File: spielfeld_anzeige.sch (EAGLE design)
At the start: 32 parts, among them IC1 UDN2981A, IC2 UDN2981A, IC3 74HC595N, IC4 74HC595N, IC5 74HC595N

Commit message: Layout fertig
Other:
- note removed: "colon data better here?!"
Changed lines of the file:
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@@
 <grid distance="0.1" unitdist="inch" unit="inch" style="lines" multiple="1" display="no" altdistance="0.01" altunitdist="inch" altunit="inch"/>
 <layers>
-<layer number="1" name="Top" color="4" fill="1" visible="yes" active="no"/>
-<layer number="16" name="Bottom" color="1" fill="1" visible="yes" active="no"/>
-<layer number="17" name="Pads" color="2" fill="1" visible="yes" active="no"/>
-<layer number="18" name="Vias" color="2" fill="1" visible="yes" active="no"/>
-<layer number="19" name="Unrouted" color="6" fill="1" visible="yes" active="no"/>
-<layer number="20" name="Dimension" color="15" fill="1" visible="yes" active="no"/>
-<layer number="21" name="tPlace" color="7" fill="1" visible="yes" active="no"/>
-<layer number="22" name="bPlace" color="7" fill="1" visible="yes" active="no"/>
-<layer number="23" name="tOrigins" color="15" fill="1" visible="yes" active="no"/>
-<layer number="24" name="bOrigins" color="15" fill="1" visible="yes" active="no"/>
-<layer number="25" name="tNames" color="7" fill="1" visible="yes" active="no"/>
-<layer number="26" name="bNames" color="7" fill="1" visible="yes" active="no"/>
-<layer number="27" name="tValues" color="7" fill="1" visible="yes" active="no"/>
-<layer number="28" name="bValues" color="7" fill="1" visible="yes" active="no"/>
+<layer number="1" name="Top" color="4" fill="1" visible="no" active="no"/>
+<layer number="16" name="Bottom" color="1" fill="1" visible="no" active="no"/>
+<layer number="17" name="Pads" color="2" fill="1" visible="no" active="no"/>
+<layer number="18" name="Vias" color="2" fill="1" visible="no" active="no"/>
+<layer number="19" name="Unrouted" color="6" fill="1" visible="no" active="no"/>
+<layer number="20" name="Dimension" color="15" fill="1" visible="no" active="no"/>
+<layer number="21" name="tPlace" color="7" fill="1" visible="no" active="no"/>
+<layer number="22" name="bPlace" color="7" fill="1" visible="no" active="no"/>
+<layer number="23" name="tOrigins" color="15" fill="1" visible="no" active="no"/>
+<layer number="24" name="bOrigins" color="15" fill="1" visible="no" active="no"/>
+<layer number="25" name="tNames" color="7" fill="1" visible="no" active="no"/>
+<layer number="26" name="bNames" color="7" fill="1" visible="no" active="no"/>
+<layer number="27" name="tValues" color="7" fill="1" visible="no" active="no"/>
+<layer number="28" name="bValues" color="7" fill="1" visible="no" active="no"/>
 <layer number="29" name="tStop" color="7" fill="3" visible="no" active="no"/>
 <layer number="30" name="bStop" color="7" fill="6" visible="no" active="no"/>
@@
 <layer number="35" name="tGlue" color="7" fill="4" visible="no" active="no"/>
 <layer number="36" name="bGlue" color="7" fill="5" visible="no" active="no"/>
-<layer number="37" name="tTest" color="7" fill="1" visible="yes" active="no"/>
-<layer number="38" name="bTest" color="7" fill="1" visible="yes" active="no"/>
+<layer number="37" name="tTest" color="7" fill="1" visible="no" active="no"/>
+<layer number="38" name="bTest" color="7" fill="1" visible="no" active="no"/>
 <layer number="39" name="tKeepout" color="4" fill="11" visible="no" active="no"/>
 <layer number="40" name="bKeepout" color="1" fill="11" visible="no" active="no"/>
@@
 <layer number="44" name="Drills" color="7" fill="1" visible="no" active="no"/>
 <layer number="45" name="Holes" color="7" fill="1" visible="no" active="no"/>
-<layer number="46" name="Milling" color="3" fill="1" visible="yes" active="no"/>
-<layer number="47" name="Measures" color="7" fill="1" visible="yes" active="no"/>
-<layer number="48" name="Document" color="7" fill="1" visible="yes" active="no"/>
-<layer number="49" name="Reference" color="7" fill="1" visible="yes" active="no"/>
-<layer number="50" name="dxf" color="7" fill="1" visible="yes" active="no"/>
-<layer number="51" name="tDocu" color="7" fill="1" visible="yes" active="no"/>
-<layer number="52" name="bDocu" color="7" fill="1" visible="yes" active="no"/>
-<layer number="53" name="tPadExt" color="7" fill="1" visible="yes" active="no"/>
-<layer number="54" name="bPadExt" color="1" fill="1" visible="yes" active="no"/>
-<layer number="56" name="wert" color="7" fill="1" visible="yes" active="no"/>
+<layer number="46" name="Milling" color="3" fill="1" visible="no" active="no"/>
+<layer number="47" name="Measures" color="7" fill="1" visible="no" active="no"/>
+<layer number="48" name="Document" color="7" fill="1" visible="no" active="no"/>
+<layer number="49" name="Reference" color="7" fill="1" visible="no" active="no"/>
+<layer number="50" name="dxf" color="7" fill="1" visible="no" active="no"/>
+<layer number="51" name="tDocu" color="7" fill="1" visible="no" active="no"/>
+<layer number="52" name="bDocu" color="7" fill="1" visible="no" active="no"/>
+<layer number="53" name="tPadExt" color="7" fill="1" visible="no" active="no"/>
+<layer number="54" name="bPadExt" color="1" fill="1" visible="no" active="no"/>
+<layer number="56" name="wert" color="7" fill="1" visible="no" active="no"/>
 <layer number="91" name="Nets" color="2" fill="1" visible="yes" active="yes"/>
 <layer number="92" name="Busses" color="1" fill="1" visible="yes" active="yes"/>
@@
 <text x="13.97" y="40.64" size="2.54" layer="97">! Dot Led orientation in schematic symbol is inverse !</text>
 <text x="-128.27" y="-44.45" size="2.54" layer="97">pnp to +5V; column driver</text>
-<text x="-157.48" y="-10.16" size="1.778" layer="97">colon data better here?!</text>
 <wire x1="-203.2" y1="-22.86" x2="-45.72" y2="-22.86" width="0.3048" layer="94"/>
 <wire x1="-45.72" y1="-22.86" x2="-45.72" y2="-43.18" width="0.3048" layer="94"/>
@@
 </sheet>
 </sheets>
+<errors>
+</errors>
 </schematic>
 </drawing>

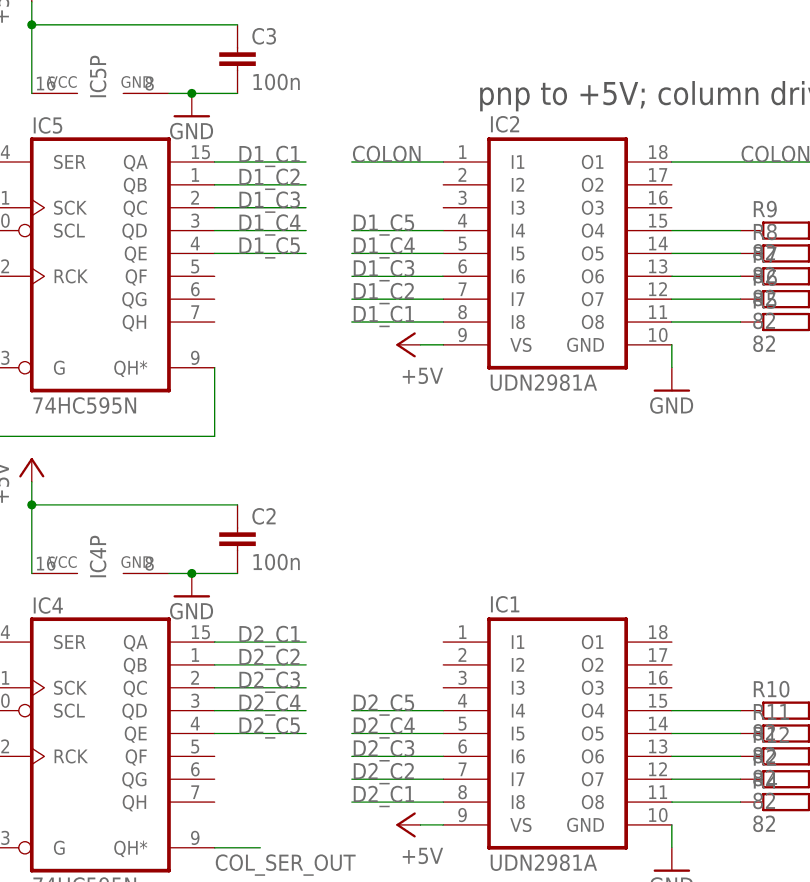
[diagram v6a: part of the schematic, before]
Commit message: Korrekturen Layout
LEDs ins mm-Raster zurückgesetzt.
Maßangaben korrigiert.
Die freien Eingänge der Treiber-ICs mit GND verbunden.
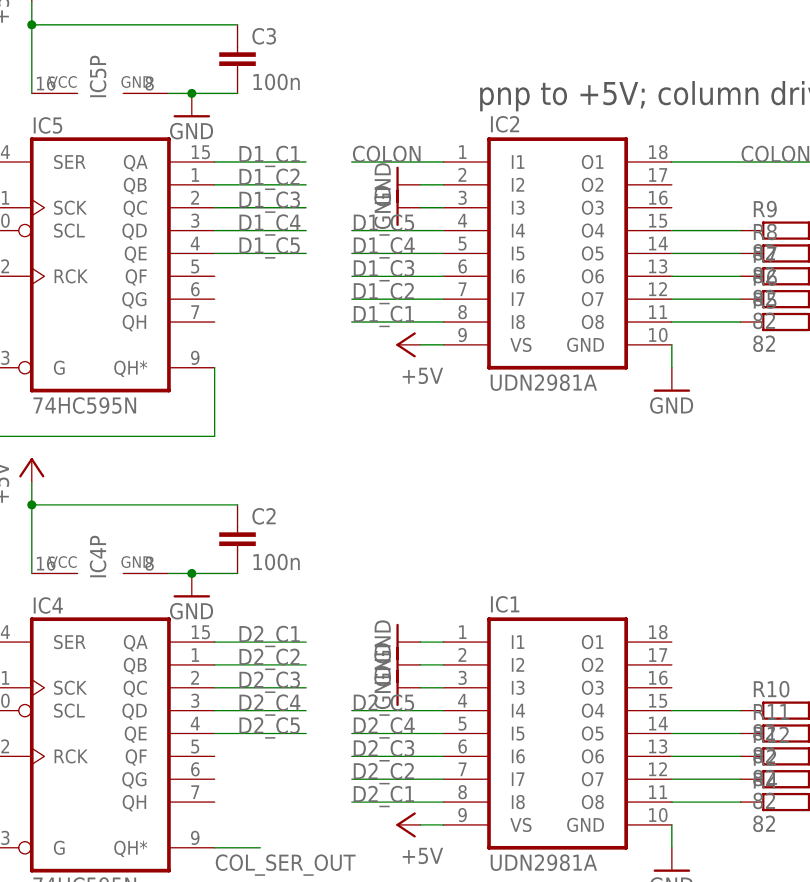
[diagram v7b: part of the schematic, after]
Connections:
- net GND: now also IC1.I1, IC1.I2, IC1.I3, IC2.I2, IC2.I3
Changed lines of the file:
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@@
 <part name="R11" library="rcl" deviceset="R-EU_" device="R0805" value="82"/>
 <part name="R12" library="rcl" deviceset="R-EU_" device="R0805" value="82"/>
+<part name="GND9" library="supply1" deviceset="GND" device=""/>
+<part name="GND10" library="supply1" deviceset="GND" device=""/>
+<part name="GND11" library="supply1" deviceset="GND" device=""/>
+<part name="GND12" library="supply1" deviceset="GND" device=""/>
+<part name="GND14" library="supply1" deviceset="GND" device=""/>
 </parts>
 <sheets>
@@
 <instance part="R11" gate="G$1" x="-93.98" y="-114.3"/>
 <instance part="R12" gate="G$1" x="-93.98" y="-116.84"/>
+<instance part="GND9" gate="1" x="-137.16" y="-53.34" rot="R270"/>
+<instance part="GND10" gate="1" x="-137.16" y="-55.88" rot="R270"/>
+<instance part="GND11" gate="1" x="-137.16" y="-104.14" rot="R270"/>
+<instance part="GND12" gate="1" x="-137.16" y="-106.68" rot="R270"/>
+<instance part="GND14" gate="1" x="-137.16" y="-109.22" rot="R270"/>
 </instances>
 <busses>
@@
 <pinref part="X1" gate="-1" pin="KL"/>
 </segment>
+<segment>
+<pinref part="IC2" gate="1" pin="I2"/>
+<pinref part="GND9" gate="1" pin="GND"/>
+<wire x1="-134.62" y1="-53.34" x2="-132.08" y2="-53.34" width="0.1524" layer="91"/>
+</segment>
+<segment>
+<pinref part="IC2" gate="1" pin="I3"/>
+<pinref part="GND10" gate="1" pin="GND"/>
+<wire x1="-134.62" y1="-55.88" x2="-132.08" y2="-55.88" width="0.1524" layer="91"/>
+</segment>
+<segment>
+<pinref part="IC1" gate="1" pin="I1"/>
+<pinref part="GND11" gate="1" pin="GND"/>
+<wire x1="-134.62" y1="-104.14" x2="-132.08" y2="-104.14" width="0.1524" layer="91"/>
+</segment>
+<segment>
+<pinref part="IC1" gate="1" pin="I2"/>
+<pinref part="GND12" gate="1" pin="GND"/>
+<wire x1="-134.62" y1="-106.68" x2="-132.08" y2="-106.68" width="0.1524" layer="91"/>
+</segment>
+<segment>
+<pinref part="IC1" gate="1" pin="I3"/>
+<pinref part="GND14" gate="1" pin="GND"/>
+<wire x1="-134.62" y1="-109.22" x2="-132.08" y2="-109.22" width="0.1524" layer="91"/>
+</segment>
 </net>
